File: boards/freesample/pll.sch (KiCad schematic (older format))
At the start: 0 parts

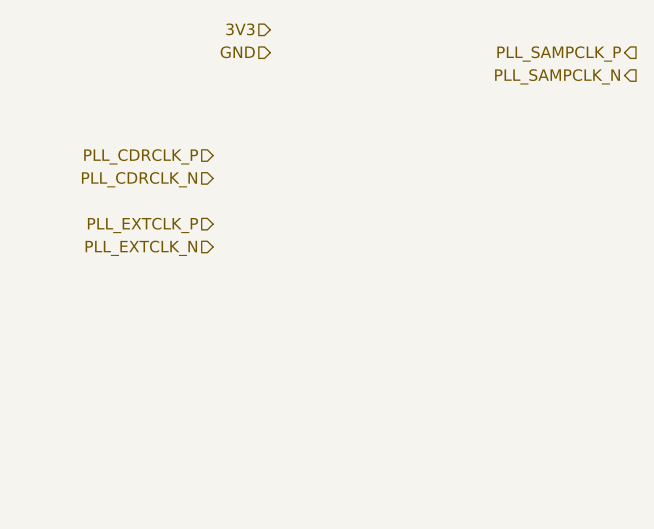
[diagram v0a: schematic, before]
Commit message: Continued initial schematic capture
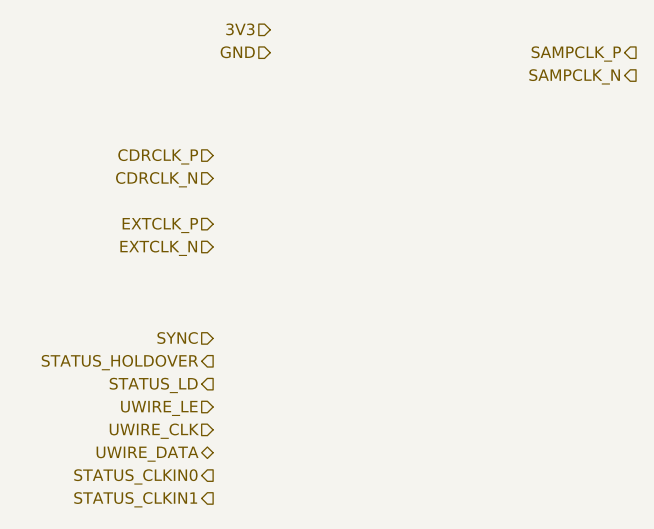
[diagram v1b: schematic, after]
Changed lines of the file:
@@
 $Descr A4 11693 8268
 encoding utf-8
-Sheet 5 11
+Sheet 5 12
 Title "FREESAMPLE Oscilloscope"
-Date "2018-12-15"
+Date "2018-12-17"
 Rev "0.1"
 Comp "Andrew D. Zonenberg / Antikernel Labs"
@@
 $EndDescr
 Text HLabel 4400 2350 0    50   Input ~ 0
-PLL_CDRCLK_P
+CDRCLK_P
 Text HLabel 4400 2450 0    50   Input ~ 0
-PLL_CDRCLK_N
+CDRCLK_N
 Text HLabel 4400 2650 0    50   Input ~ 0
-PLL_EXTCLK_P
+EXTCLK_P
 Text HLabel 4400 2750 0    50   Input ~ 0
-PLL_EXTCLK_N
+EXTCLK_N
 Text HLabel 4650 1800 0    50   Input ~ 0
 3V3
@@
 GND
 Text HLabel 6250 1900 0    50   Output ~ 0
-PLL_SAMPCLK_P
+SAMPCLK_P
 Text HLabel 6250 2000 0    50   Output ~ 0
-PLL_SAMPCLK_N
+SAMPCLK_N
+Text HLabel 4400 3150 0    50   Input ~ 0
+SYNC
+Text HLabel 4400 3250 0    50   Output ~ 0
+STATUS_HOLDOVER
+Text HLabel 4400 3350 0    50   Output ~ 0
+STATUS_LD
+Text HLabel 4400 3450 0    50   Input ~ 0
+UWIRE_LE
+Text HLabel 4400 3550 0    50   Input ~ 0
+UWIRE_CLK
+Text HLabel 4400 3650 0    50   BiDi ~ 0
+UWIRE_DATA
+Text HLabel 4400 3750 0    50   Output ~ 0
+STATUS_CLKIN0
+Text HLabel 4400 3850 0    50   Output ~ 0
+STATUS_CLKIN1
 $EndSCHEMATC

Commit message: Continued work on schematic capture
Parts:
- added C103, C104, C105, C106, C107, C108: 4.7 uF, symbol device:C
- added C109, C110, C111, C112, C113, C115, C117, C118, C120, C122, C123, C125, C126: 0.47 uF, symbol device:C
- added C114: LF1_C1_TBD, symbol device:C
- added C116: LF1_C2_TBD, symbol device:C
- added C119: LF2_C1_TBD, symbol device:C
- added C121: LF2_C2_TBD, symbol device:C
- added C124: C, symbol device:C
- added C127: 10 uF, symbol device:C
- added C128: 0.1 uF, symbol device:C
- added FB5, FB6: TBD, symbol passive-azonenberg:INDUCTOR_PWROUT
- added R14: LF1_R2_TBD, symbol device:R
- added R15: LF2_R2_TBD, symbol device:R
- added U14: LMK04806, symbol special-azonenberg:LMK04806
- added U15: ASG-D-V-A-125.000MHZ, symbol osc-azonenberg:OSC_LVDS_VCXO
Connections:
- net 3V3: now also C103.1, C104.1, C105.1, C106.1, C109.1, C112.1, C113.1, C115.1, C117.1, C118.1, C120.1, C122.1, C123.1, C124.2, C125.1, C126.1, FB5.2, FB6.2, U14.10 (VCC_VCO), U14.17 (VCC_CLK23), U14.18 (VCC_CLK45), U14.24 (VCC_D), U14.30 (VCC_CLKIN), U14.38 (VCC_PLL2), U14.43 (VCC_PLL2), U14.47 (VCC_CLKOUT67), U14.52 (VCC_CLKOUT89), U14.57 (VCC_CLKOUT1011), U14.64 (VCC_CLKOUT02), U15.2 (EN), U15.6 (VDD)
- net CDRCLK_N: now also U14.29 (CLKIN0_N)
- net CDRCLK_P: now also U14.28 (CLKIN0_P)
- net EXTCLK_N: now also U14.26 (CLKIN1_N)
- net EXTCLK_P: now also U14.25 (CLKIN1_P)
- net GND: now also C103.2, C104.2, C105.2, C106.2, C107.2, C108.2, C109.2, C110.2, C111.2, C112.2, C113.2, C114.2, C115.2, C117.2, C118.2, C119.2, C120.2, C122.2, C123.2, C124.1, C125.2, C126.2, C127.1, C128.1, R14.2, R15.2, U14.23 (GND), U14.PAD (GND), U15.3 (GND)
- net SAMPCLK_N: now also U14.2 (CLKOUT0_N)
- net SAMPCLK_P: now also U14.1 (CLKOUT0_P)
- net STATUS_CLKIN0: now also U14.62 (STATUS_CLKIN0)
- net STATUS_CLKIN1: now also U14.63 (STATUS_CLKIN1)
- net STATUS_HOLDOVER: now also U14.27 (STATUS_HOLDOVER)
- net STATUS_LD: now also U14.33 (STATUS_LD)
- net SYNC: now also U14.6 (SYNC)
- net UWIRE_CLK: now also U14.45 (UWIRE_CLK)
- net UWIRE_DATA: now also U14.46 (UWIRE_DATA)
- net UWIRE_LE: now also U14.44 (UWIRE_LE)
- new net: C127.2, U14.11 (LDObyp1)
- new net: C128.2, U14.12 (LDObyp2)
- new net: C116.2, R14.1
- new net: C121.2, R15.1
- new net PLL1_CLK_N: U14.37 (OSCIN_N), U15.5 (OUT_N)
- new net PLL1_CLK_P: U14.36 (OSCIN_P), U15.4 (OUT_P)
- new net PLL_CP1: C114.1, C116.1, U14.34 (CPOUT1), U15.1 (CTL)
- new net PLL_CP2: C119.1, C121.1, U14.42 (CPOUT2)
- new net VCC_CP1: C107.1, C110.1, FB5.1, U14.35 (VCC_PLL1_CP1)
- new net VCC_CP2: C108.1, C111.1, FB6.1, U14.41 (VCC_PLL2_CP2)
- no-connect marks 0 -> 26
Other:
- note added: "PLL1 loop filter\nNeed to calculate values"
- note added: "PLL2 loop filter\nNeed to calculate values"

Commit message: Continued schematic capture work. Hooked up most SoM connectors.
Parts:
- C114: value LF1_C1_TBD -> 1 uF
- C116: value LF1_C2_TBD -> 47 uF
- C119: value LF2_C1_TBD -> 27 pF
- C121: value LF2_C2_TBD -> 2700 pF
- R14: value LF1_R2_TBD -> 150
- R15: value LF2_R2_TBD -> 1K 1%
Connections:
- net FPGACLK_P: now reaches U14.13 (CLKOUT2_P)
- net FPGACLK_N: now reaches U14.14 (CLKOUT2_N)
- no-connect marks 26 -> 24
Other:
- note added: "PLL CONFIGURATION\nLoop 1\n 1.6 mA charge pump gain\n 25 MHz phase det\nLoop 2\n 3.2 mA charge pump gain\n 2.5 GHz Fvco\n 50 MHz PFD\n C3/C4 = 0.01 nF\n R3/R4 = 0.2K"
- note added: "PLL1 loop filter"
- note added: "PLL2 loop filter"
- note removed: "PLL1 loop filter\nNeed to calculate values"
- note removed: "PLL2 loop filter\nNeed to calculate values"
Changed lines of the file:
@@
 Sheet 5 12
 Title "FREESAMPLE Oscilloscope"
-Date "2019-02-26"
+Date "2019-03-10"
 Rev "0.1"
 Comp "Andrew D. Zonenberg / Antikernel Labs"
 Comment1 "PLL for clock synthesis and coarse phasing for X sampling point position"
-Comment2 ""
+Comment2 "Ready for review"
 Comment3 ""
 Comment4 ""
@@
 NoConn ~ 10250 1250
 NoConn ~ 10250 1350
-NoConn ~ 10250 1550
-NoConn ~ 10250 1650
 NoConn ~ 10250 1850
 NoConn ~ 10250 1950
@@
 NoConn ~ 10250 4850
 NoConn ~ 10250 4950
-$Comp
-L device:C C114
-U 1 1 5C93D973
-P 3550 3250
-F 0 "C114" H 3665 3296 50  0000 L CNN
-F 1 "LF1_C1_TBD" H 3665 3205 50  0000 L CNN
-F 2 "" H 3588 3100 50  0001 C CNN
-F 3 "" H 3550 3250 50  0001 C CNN
-	1    3550 3250
-	1    0    0    -1
-$EndComp
 Text Label 3100 2650 0    50   ~ 0
 PLL_CP1
@@
 P 4250 3250
 F 0 "C116" H 4365 3296 50  0000 L CNN
-F 1 "LF1_C2_TBD" H 4365 3205 50  0000 L CNN
+F 1 "47 uF" H 4365 3205 50  0000 L CNN
 F 2 "" H 4288 3100 50  0001 C CNN
 F 3 "" H 4250 3250 50  0001 C CNN
@@
 P 4250 3550
 F 0 "R14" H 4320 3596 50  0000 L CNN
-F 1 "LF1_R2_TBD" H 4320 3505 50  0000 L CNN
+F 1 "150" H 4320 3505 50  0000 L CNN
 F 2 "" V 4180 3550 50  0001 C CNN
 F 3 "" H 4250 3550 50  0001 C CNN
@@
 Wire Wire Line
 	3550 3100 4250 3100
-Text Notes 3550 3900 0    50   ~ 0
-PLL1 loop filter\nNeed to calculate values
+Text Notes 3550 3800 0    50   ~ 0
+PLL1 loop filter
 $Comp
 L device:C C119
@@
 P 5150 3250
 F 0 "C119" H 5265 3296 50  0000 L CNN
-F 1 "LF2_C1_TBD" H 5265 3205 50  0000 L CNN
+F 1 "27 pF" H 5265 3205 50  0000 L CNN
 F 2 "" H 5188 3100 50  0001 C CNN
 F 3 "" H 5150 3250 50  0001 C CNN
@@
 P 5850 3250
 F 0 "C121" H 5965 3296 50  0000 L CNN
-F 1 "LF2_C2_TBD" H 5965 3205 50  0000 L CNN
+F 1 "2700 pF" H 5965 3205 50  0000 L CNN
 F 2 "" H 5888 3100 50  0001 C CNN
 F 3 "" H 5850 3250 50  0001 C CNN
@@
 P 5850 3550
 F 0 "R15" H 5920 3596 50  0000 L CNN
-F 1 "LF2_R2_TBD" H 5920 3505 50  0000 L CNN
+F 1 "1K 1%" H 5920 3505 50  0000 L CNN
 F 2 "" V 5780 3550 50  0001 C CNN
 F 3 "" H 5850 3550 50  0001 C CNN
@@
 Wire Wire Line
 	5150 3100 5850 3100
-Text Notes 5150 3900 0    50   ~ 0
-PLL2 loop filter\nNeed to calculate values
+Text Notes 5150 3800 0    50   ~ 0
+PLL2 loop filter
 $Comp
 L osc-azonenberg:OSC_LVDS_VCXO U15
@@
 Wire Wire Line
 	3600 2050 3600 2150
+Text Notes 4650 1650 0    50   ~ 0
+PLL CONFIGURATION\nLoop 1\n  1.6 mA charge pump gain\n  25 MHz phase det\nLoop 2\n  3.2 mA charge pump gain\n  2.5 GHz Fvco\n  50 MHz PFD\n  C3/C4 = 0.01 nF\n  R3/R4 = 0.2K
+$Comp
+L device:C C114
+U 1 1 5C93D973
+P 3550 3250
+F 0 "C114" H 3665 3296 50  0000 L CNN
+F 1 "1 uF" H 3665 3205 50  0000 L CNN
+F 2 "" H 3588 3100 50  0001 C CNN
+F 3 "" H 3550 3250 50  0001 C CNN
+	1    3550 3250
+	1    0    0    -1
+$EndComp
+Text HLabel 10250 1550 2    50   Output ~ 0
+FPGACLK_P
+Text HLabel 10250 1650 2    50   Output ~ 0
+FPGACLK_N
 $EndSCHEMATC

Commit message: Finished PSU schematic. Ready for design review!
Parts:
- added J13, J14: SMA, symbol Connector:Conn_Coaxial
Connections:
- net GND: now also J13.2 (Ext), J14.2 (Ext)
- net PLLOUT_P: now reaches U14.19 (CLKOUT4_P)
- net PLLOUT_P: now also J13.1 (In)
- net PLLOUT_N: now reaches U14.20 (CLKOUT4_N)
- net PLLOUT_N: now also J14.1 (In)
- no-connect marks 24 -> 22
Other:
- note added: "PLL clock out\nfor debugging"
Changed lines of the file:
@@
 Sheet 5 12
 Title "FREESAMPLE Oscilloscope"
-Date "2019-03-10"
+Date "2019-03-11"
 Rev "0.1"
 Comp "Andrew D. Zonenberg / Antikernel Labs"
@@
 NoConn ~ 10250 1850
 NoConn ~ 10250 1950
-NoConn ~ 10250 2150
-NoConn ~ 10250 2250
 NoConn ~ 10250 2450
 NoConn ~ 10250 2550
@@
 Text HLabel 10250 1650 2    50   Output ~ 0
 FPGACLK_N
+$Comp
+L Connector:Conn_Coaxial J14
+U 1 1 5D284EDA
+P 10900 2300
+F 0 "J14" H 11000 2275 50  0000 L CNN
+F 1 "SMA" H 11000 2184 50  0000 L CNN
+F 2 "" H 10900 2300 50  0001 C CNN
+F 3 "" H 10900 2300 50  0001 C CNN
+	1    10900 2300
+	1    0    0    -1
+$EndComp
+$Comp
+L Connector:Conn_Coaxial J13
+U 1 1 5D286A97
+P 10900 2100
+F 0 "J13" H 11000 1982 50  0000 L CNN
+F 1 "SMA" H 11000 2073 50  0000 L CNN
+F 2 "" H 10900 2100 50  0001 C CNN
+F 3 "" H 10900 2100 50  0001 C CNN
+	1    10900 2100
+	1    0    0    1
+$EndComp
+Wire Wire Line
+	10250 2150 10750 2150
+Wire Wire Line
+	10750 2150 10750 2100
+Wire Wire Line
+	10250 2250 10750 2250
+Wire Wire Line
+	10750 2250 10750 2300
+Text Label 10900 1900 0    50   ~ 0
+GND
+Text Label 10900 2500 0    50   ~ 0
+GND
+Text Label 10250 2150 0    50   ~ 0
+PLLOUT_P
+Text Label 10250 2250 0    50   ~ 0
+PLLOUT_N
+Text Notes 10600 2700 0    50   ~ 0
+PLL clock out\nfor debugging
 $EndSCHEMATC

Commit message: Began design review. Added review status checklist with current progress. Added some test points, plus an attenuator on the DAC output to prevent bad firmware from damaging the comparators
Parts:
- added J22, J23: SMA, symbol Connector:Conn_Coaxial
- C124: value C -> 0.47 uF
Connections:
- net GND: now also J22.2 (Ext), J23.2 (Ext)
- net OSCOUT_P: now reaches U14.31 (OSCOUT1_P)
- net OSCOUT_P: now also J22.1 (In)
- net OSCOUT_N: now reaches U14.32 (OSCOUT1_N)
- net OSCOUT_N: now also J23.1 (In)
- no-connect marks 22 -> 20
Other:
- note added: "Debug test point"
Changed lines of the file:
@@
 NoConn ~ 10250 4550
 NoConn ~ 10250 4650
-NoConn ~ 10250 4850
-NoConn ~ 10250 4950
 Text Label 3100 2650 0    50   ~ 0
 PLL_CP1
@@
 Wire Wire Line
 	6800 1450 6900 1450
-Wire Wire Line
-	6800 1450 6800 1550
-Wire Wire Line
-	6800 1550 6900 1550
 Text Label 6800 1750 2    50   ~ 0
 PLL_CP1
@@
 P 6800 1200
 F 0 "C124" H 6915 1246 50  0000 L CNN
-F 1 "C" H 6915 1155 50  0000 L CNN
+F 1 "0.47 uF" H 6915 1155 50  0000 L CNN
 F 2 "" H 6838 1050 50  0001 C CNN
 F 3 "" H 6800 1200 50  0001 C CNN
@@
 Text Notes 10600 2700 0    50   ~ 0
 PLL clock out\nfor debugging
+$Comp
+L Connector:Conn_Coaxial J23
+U 1 1 5D52905E
+P 10900 5000
+F 0 "J23" H 11000 4975 50  0000 L CNN
+F 1 "SMA" H 11000 4884 50  0000 L CNN
+F 2 "" H 10900 5000 50  0001 C CNN
+F 3 "" H 10900 5000 50  0001 C CNN
+	1    10900 5000
+	1    0    0    -1
+$EndComp
+$Comp
+L Connector:Conn_Coaxial J22
+U 1 1 5D529068
+P 10900 4800
+F 0 "J22" H 11000 4682 50  0000 L CNN
+F 1 "SMA" H 11000 4773 50  0000 L CNN
+F 2 "" H 10900 4800 50  0001 C CNN
+F 3 "" H 10900 4800 50  0001 C CNN
+	1    10900 4800
+	1    0    0    1
+$EndComp
+Wire Wire Line
+	10250 4850 10750 4850
+Wire Wire Line
+	10750 4850 10750 4800
+Wire Wire Line
+	10250 4950 10750 4950
+Wire Wire Line
+	10750 4950 10750 5000
+Text Label 10900 4600 0    50   ~ 0
+GND
+Text Label 10900 5200 0    50   ~ 0
+GND
+Text Label 10250 4850 0    50   ~ 0
+OSCOUT_P
+Text Label 10250 4950 0    50   ~ 0
+OSCOUT_N
+Text Notes 10350 5300 0    50   ~ 0
+Debug test point
 $EndSCHEMATC
